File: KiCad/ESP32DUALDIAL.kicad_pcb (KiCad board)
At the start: 2 copper layers, 180.5 x 74 mm, 53 parts, among them J1 SERVICE, J2 Conn_01x04_Male, J3 FAN, J4 FAN, J5 Conn_01x03_Male, J6 Conn_01x02_Male, J7 Conn_01x02_Male, J8 Conn_01x02_Male, Q1 Q_NMOS_GDS, SW1 Rotary_Encoder_Switch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

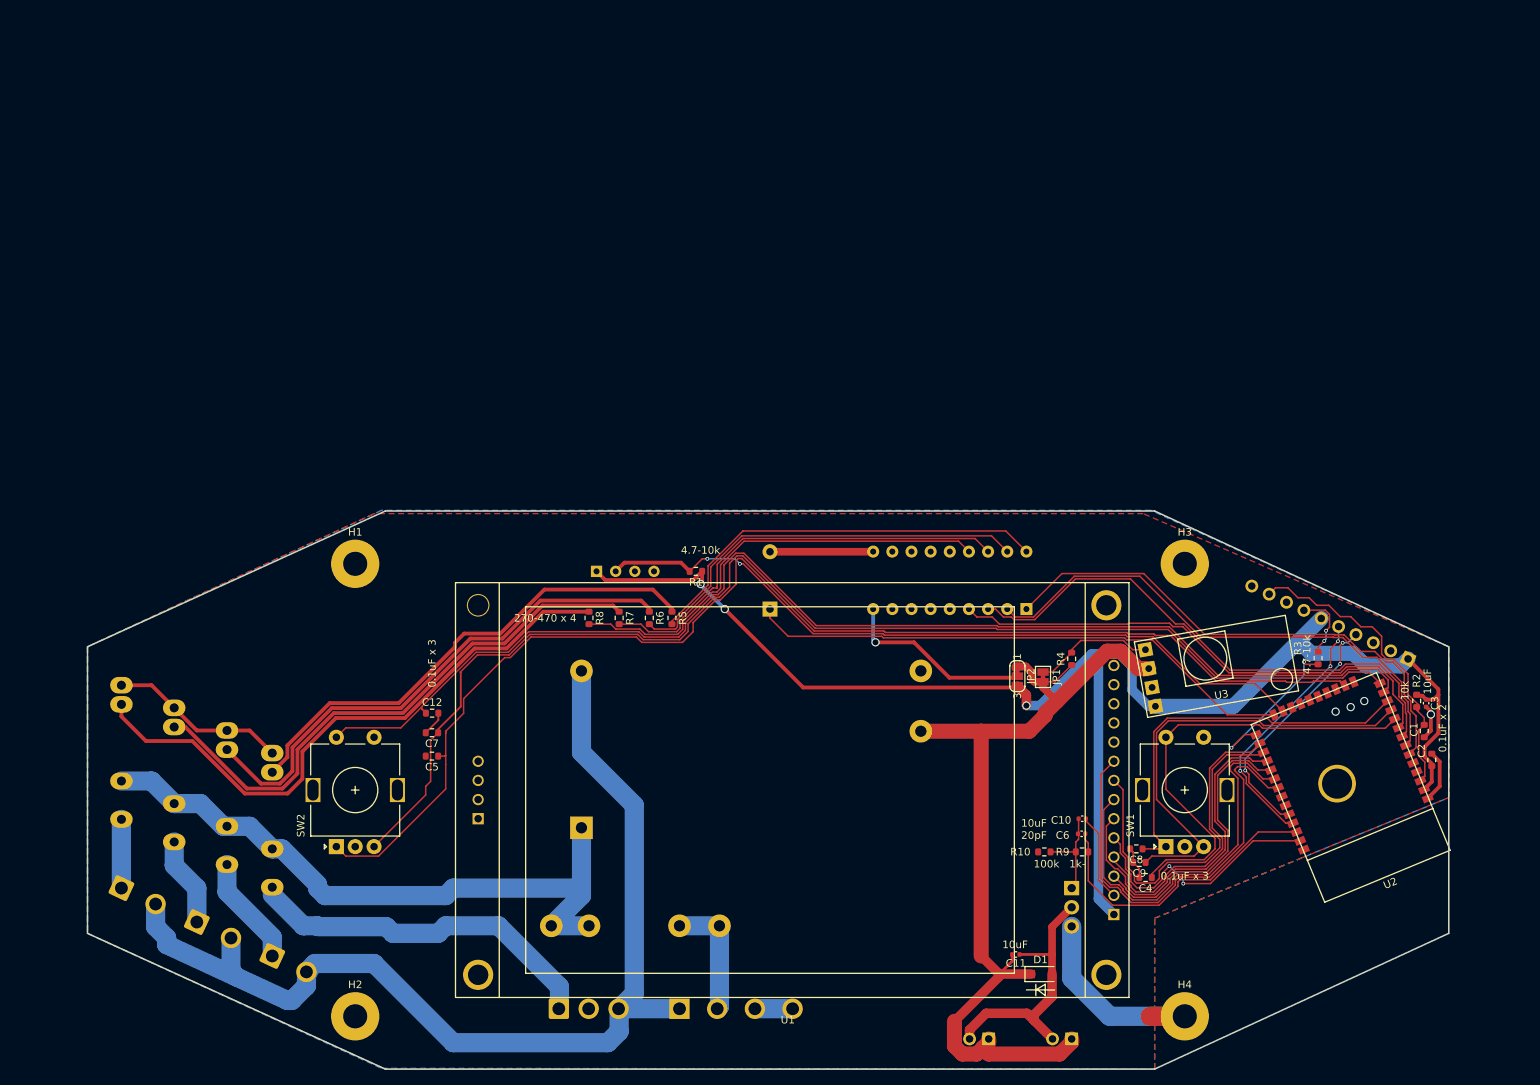
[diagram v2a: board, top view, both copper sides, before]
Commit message: fix GPIO assign bug.
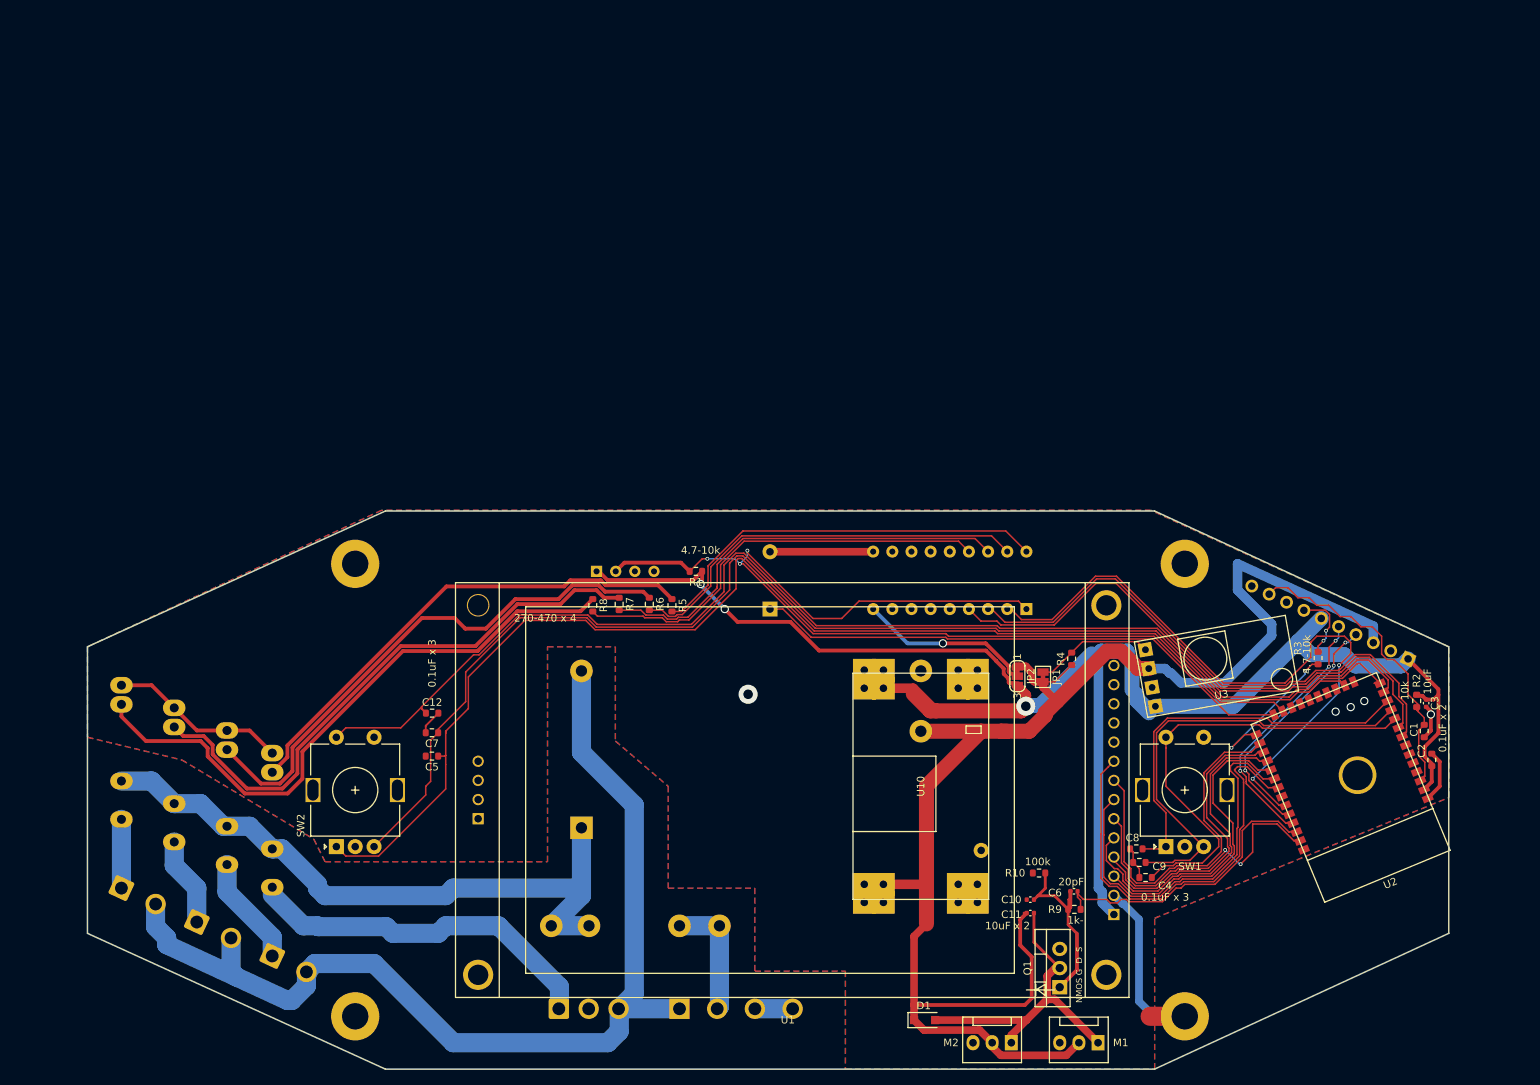
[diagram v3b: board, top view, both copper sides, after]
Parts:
- removed J3, J4: FAN, Connector_PinSocket_2.54mm:PinSocket_1x02_P2.54mm_Vertical
- added M1: Fan_CPU_4pin, Connector:FanPinHeader_1x03_P2.54mm_Vertical, F.Cu at (158.5, 143.5)
- added M2: Fan_CPU_4pin, Connector:FanPinHeader_1x03_P2.54mm_Vertical, F.Cu at (147.0, 143.5)
- added U10: Mini560_DC-DC_JW5068A, library:Mini560_DC-DC_JW5068A, F.Cu at (135.0, 109.5)
- Q1: moved to F.Cu
- moved D1 16.7 mm to (135.5, 140.5)
- moved Q1 13.2 mm to (153.4, 136.1), turned to 90 degrees
- moved C10 12.7 mm to (149.5, 124.5), turned to 0 degrees
- moved C6 7.69 mm to (155.3, 123.4)
- moved R9 7.69 mm to (155.4, 125.8)
- moved C11 5.82 mm to (149.5, 126.3)
- moved R10 2.89 mm to (150.7, 121.0)
- moved R6 1.85 mm to (99.0, 85.3)
- moved R7 1.85 mm to (95.0, 85.3)
- moved R8 1.75 mm to (91.5, 85.5)
- moved R5 1.67 mm to (102.0, 85.5)
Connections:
- J1 pad 3: Net-(J1-Pad3) -> +12V
- R1 pad 2: Net-(R1-Pad2) -> PUMP
- U2 pad 23: Net-(R1-Pad2) -> PUMP
- U2 pad 28: Net-(U1-Pad6) -> Net-(U1-Pad5)
- U2 pad 33: Net-(U2-Pad33) -> OZON0
- U2 pad 37: Net-(U1-Pad5) -> Net-(U1-Pad6)
- U2 pad 6: PUMP -> Net-(U2-Pad6)
- U2 pad 7: OZON0 -> Net-(U2-Pad7)
- U4 pad 2: Net-(R1-Pad2) -> PUMP
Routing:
- net Net-(R1-Pad2): track 98.5 -> 0.00 mm, vias 2 -> 0
- net +12V: track 120.6 -> 213.6 mm
- net PUMP: track 69.2 -> 142.9 mm, vias 0 -> 3
- net +3V3: track 195.0 -> 234.0 mm
- net OZON0: track 69.9 -> 87.7 mm, vias 0 -> 2
- net GND: track 97.0 -> 84.2 mm, vias 4 -> 5
- net Net-(C10-Pad2): track 12.9 -> 25.1 mm
- net Net-(U1-Pad5): track 34.8 -> 44.5 mm, vias 2 -> 0
- net OZON2: track 67.9 -> 75.1 mm
- net Net-(C11-Pad1): track 35.9 -> 42.9 mm
- net Net-(U1-Pad6): track 45.7 -> 40.1 mm, vias 0 -> 2
- net Net-(C5-Pad1): track 167.8 -> 171.1 mm
- net OZON1: track 71.4 -> 74.6 mm
- net Net-(C12-Pad1): track 163.5 -> 166.3 mm
- net Net-(C7-Pad1): track 167.7 -> 170.4 mm
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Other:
- board text added: "100k"
- board text added: "10uF x 2"
- board text added: "1k-"
- board text added: "20pF"
- board text added: "3V3 GND 12V RXD TXD 3V3 PRG GND RST GND"
- board text added: "NMOS G D S"
- board text removed: "100k 1k-"
- board text removed: "10uF 20pF"
- board text removed: "3V3 GND KEY RXD TXD 3V3 PRG GND RST GND"
- board text removed: "G D S NMOS"

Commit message: change to ROTARY ENCODER chattaling fix. and many change...
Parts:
- added R11: 270, Resistor_SMD:R_0603_1608Metric, F.Cu at (170.2, 100.5)
- added R12: 270, Resistor_SMD:R_0603_1608Metric, F.Cu at (177.6, 99.2)
- added R13: 270, Resistor_SMD:R_0603_1608Metric, F.Cu at (173.9, 99.8)
- added R14: 270, Resistor_SMD:R_0603_1608Metric, F.Cu at (94.2, 86.2)
- added R15: 270, Resistor_SMD:R_0603_1608Metric, F.Cu at (96.8, 86.2)
- added R16: 270, Resistor_SMD:R_0603_1608Metric, F.Cu at (99.4, 86.2)
- added R17: 10k, Resistor_SMD:R_0603_1608Metric, F.Cu at (172.9, 87.0)
- added R18: 10k, Resistor_SMD:R_0603_1608Metric, F.Cu at (177.7, 87.0)
- added R19: 10k, Resistor_SMD:R_0603_1608Metric, F.Cu at (158.8, 79.8)
- added R20: 10k, Resistor_SMD:R_0603_1608Metric, F.Cu at (175.3, 87.0)
- added R21: 10k, Resistor_SMD:R_0603_1608Metric, F.Cu at (162.8, 79.7)
- added R22: 10k, Resistor_SMD:R_0603_1608Metric, F.Cu at (154.8, 79.8)
- R3: value 4.7k -> 10k
- R5, R6, R7, R8: value 330 -> 270
- moved C4 18.8 mm to (164.4, 102.8)
- moved R3 18.1 mm to (170.4, 87.0)
- moved R5 12.0 mm to (90.0, 85.5)
- moved R6 11.5 mm to (87.5, 85.5)
- moved R7 10.0 mm to (85.0, 85.5)
- moved R8 9.00 mm to (82.5, 85.5)
- moved C9 7.99 mm to (171.9, 120.6)
- moved C8 5.49 mm to (168.3, 120.6), turned to 0 degrees
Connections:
- R1 pad 2: PUMP -> Net-(R1-Pad2)
- U2 pad 10: Net-(C4-Pad1) -> Net-(R11-Pad2)
- U2 pad 11: Net-(C9-Pad1) -> OZON0
- U2 pad 12: Net-(C8-Pad1) -> PUMP
- U2 pad 13: Net-(C12-Pad1) -> Net-(R14-Pad2)
- U2 pad 14: Net-(C7-Pad1) -> Net-(R15-Pad2)
- U2 pad 16: Net-(C5-Pad1) -> Net-(R16-Pad2)
- U2 pad 23: PUMP -> Net-(R1-Pad2)
- U2 pad 33: OZON0 -> Net-(U2-Pad33)
- U4 pad 2: PUMP -> Net-(R1-Pad2)
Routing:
- net Net-(R14-Pad2): track 0.00 -> 126.7 mm, vias 0 -> 2
- net Net-(R15-Pad2): track 0.00 -> 122.9 mm, vias 0 -> 2
- net Net-(C12-Pad1): track 166.3 -> 44.8 mm
- net Net-(R16-Pad2): track 0.00 -> 118.1 mm, vias 0 -> 2
- net Net-(C7-Pad1): track 170.4 -> 53.7 mm
- net Net-(C5-Pad1): track 171.1 -> 63.9 mm
- net Net-(R1-Pad2): track 0.00 -> 107.1 mm, vias 0 -> 2
- net PUMP: track 142.9 -> 56.4 mm, vias 3 -> 0
- net +3V3: track 234.0 -> 308.8 mm, vias 3 -> 5
- net Net-(C4-Pad1): track 59.9 -> 5.79 mm
- net Net-(R13-Pad2): track 0.00 -> 43.3 mm, vias 0 -> 2
- net Net-(R11-Pad2): track 0.00 -> 43.2 mm, vias 0 -> 2
- net Net-(R12-Pad2): track 0.00 -> 39.0 mm, vias 0 -> 2
- net Net-(C9-Pad1): track 60.1 -> 25.2 mm, vias 0 -> 2
- net Net-(C8-Pad1): track 52.5 -> 25.4 mm, vias 0 -> 2
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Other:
- board text added: "10k x 3"
- board text added: "10k x 4"
- board text added: "270 x 3"
- board text added: "270-470 x 7"
- board text added: "URN-X V5"
- board text removed: "270-470 x 4"

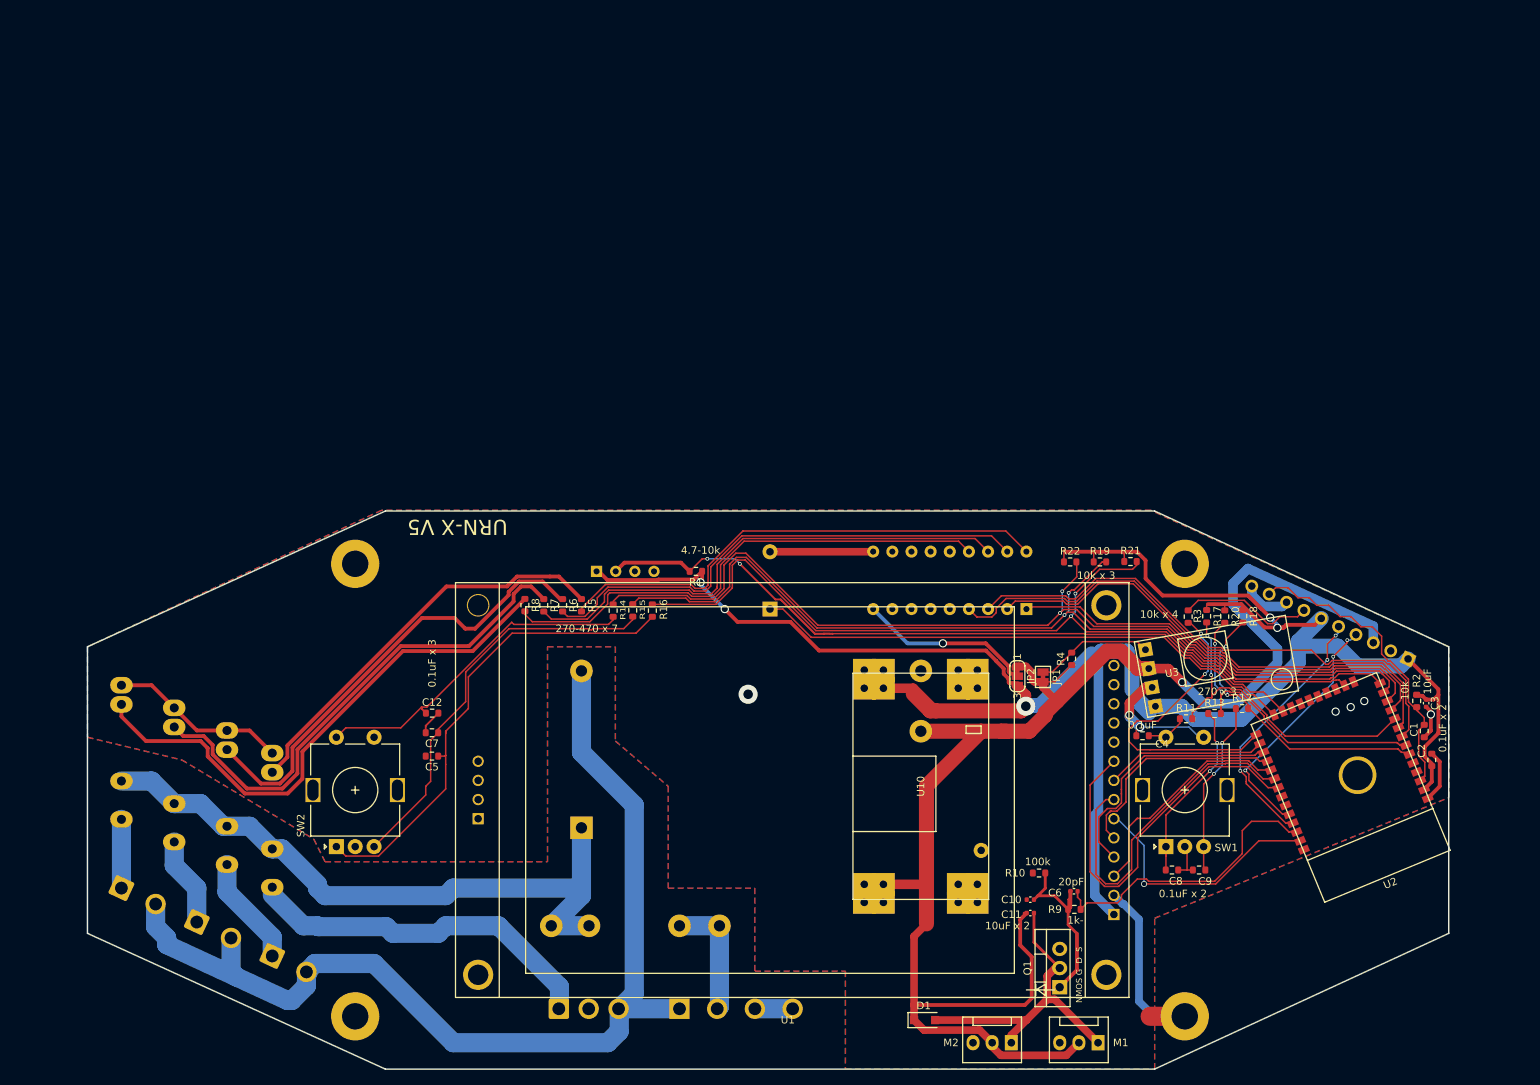
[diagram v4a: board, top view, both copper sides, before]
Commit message: Ver.6 : Add test pads / NNC and SHARP SSR both support / mode jumper
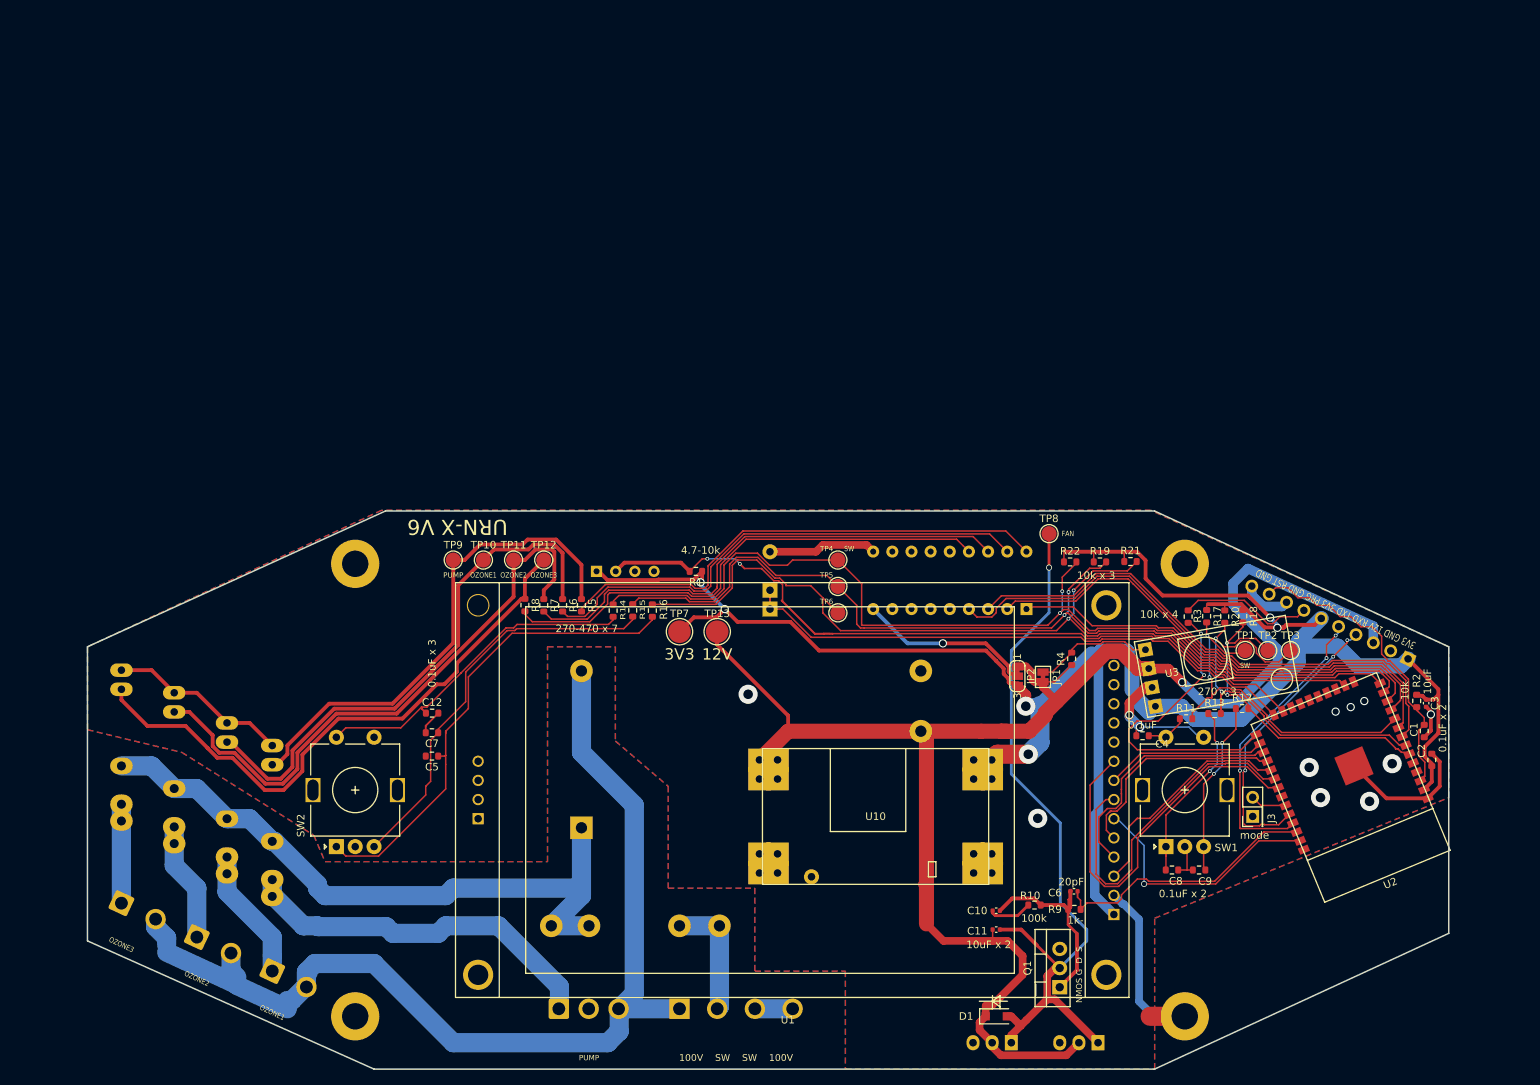
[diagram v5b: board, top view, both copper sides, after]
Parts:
- added J3: mode, Connector_PinHeader_2.54mm:PinHeader_2x01_P2.54mm_Vertical, F.Cu at (179.0, 113.5)
- added TP1: TestPoint, TestPoint:TestPoint_Pad_D2.0mm, F.Cu at (178.0, 91.5)
- added TP10: TestPoint, TestPoint:TestPoint_Pad_D2.0mm, F.Cu at (77.0, 79.5)
- added TP11: TestPoint, TestPoint:TestPoint_Pad_D2.0mm, F.Cu at (81.0, 79.5)
- added TP12: TestPoint, TestPoint:TestPoint_Pad_D2.0mm, F.Cu at (85.0, 79.5)
- added TP13: TestPoint, TestPoint:TestPoint_Pad_D3.0mm, F.Cu at (108.0, 89.0)
- added TP2: TestPoint, TestPoint:TestPoint_Pad_D2.0mm, F.Cu at (181.0, 91.5)
- added TP3: TestPoint, TestPoint:TestPoint_Pad_D2.0mm, F.Cu at (184.0, 91.5)
- added TP4: TestPoint, TestPoint:TestPoint_Pad_D2.0mm, F.Cu at (124.0, 79.5)
- added TP5: TestPoint, TestPoint:TestPoint_Pad_D2.0mm, F.Cu at (124.0, 83.0)
- added TP6: TestPoint, TestPoint:TestPoint_Pad_D2.0mm, F.Cu at (124.0, 86.5)
- added TP7: TestPoint, TestPoint:TestPoint_Pad_D3.0mm, F.Cu at (103.0, 89.0)
- added TP8: TestPoint, TestPoint:TestPoint_Pad_D2.0mm, F.Cu at (152.0, 76.0)
- added TP9: TestPoint, TestPoint:TestPoint_Pad_D2.0mm, F.Cu at (73.0, 79.5)
- BZ1: footprint Buzzer_Beeper:Buzzer_12x9.5RM7.6 -> library:Buzzer_7.6_5.0
- M1, M2: moved to B.Cu
- U5, U6, U7, U8: footprint library:SSR_SHARP_S108T02 -> library:SSR_SHARP_S108T02_NNC_NNG1D-25mm
- moved D1 9.51 mm to (145.0, 140.0)
- moved U10 7.21 mm to (129.0, 113.5), turned to 0 degrees
- moved C11 5.02 mm to (145.0, 128.5)
- moved C10 4.75 mm to (145.0, 126.0)
- moved R10 4.29 mm to (150.1, 125.2)
- moved J6 2.00 mm to (49.0, 134.0)
- moved J7 2.00 mm to (39.0, 129.5)
- moved J8 2.00 mm to (29.0, 125.0)
- moved U7 2.00 mm to (36.0, 106.0)
- moved U8 2.00 mm to (29.0, 103.0)
- moved U5 1.00 mm to (49.0, 113.0)
- moved U6 1.00 mm to (43.0, 110.0)
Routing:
- net Net-(C11-Pad1): track 42.9 -> 100.4 mm, vias 0 -> 1
- net GND: track 110.1 -> 128.6 mm, vias 7 -> 12
- net Net-(R13-Pad2): track 43.3 -> 56.0 mm
- net Net-(R5-Pad1): track 53.9 -> 66.4 mm
- net Net-(R7-Pad1): track 67.4 -> 79.2 mm
- net +12V: track 218.1 -> 228.7 mm
- net Net-(R6-Pad1): track 61.7 -> 71.9 mm
- net +3V3: track 308.8 -> 301.5 mm, vias 5 -> 6
- net Net-(R8-Pad1): track 72.8 -> 78.5 mm
- net Net-(R11-Pad2): track 43.2 -> 48.9 mm
- net Net-(R12-Pad2): track 39.0 -> 44.6 mm
- net Net-(J1-Pad4): track 33.1 -> 38.4 mm
- net Net-(J3-Pad2): track 0.00 -> 4.80 mm
- net Net-(J1-Pad5): track 34.9 -> 39.5 mm
- net Net-(R16-Pad2): track 118.1 -> 122.5 mm
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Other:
- outline, holes or cut-outs redrawn
- board text added: "100V SW SW 100V"
- board text added: "12V"
- board text added: "3V3"
- board text added: "FAN"
- board text added: "OZONE1"
- board text added: "OZONE2"
- board text added: "OZONE3"
- board text added: "PUMP"
- board text added: "SW"
- board text added: "URN-X V6"
- board text added: "mode"
- board text removed: "URN-X V5"
